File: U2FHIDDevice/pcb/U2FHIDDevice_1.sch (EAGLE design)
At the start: 32 parts, among them CN1 TE-1734028, CN2 IF_7PIN, SW1 SKRPACE010, U1 STM32F411RET6_, U2 LD39050PU33R_DEV, U3 USBLC6-2SC6, X1 NX3215SA_

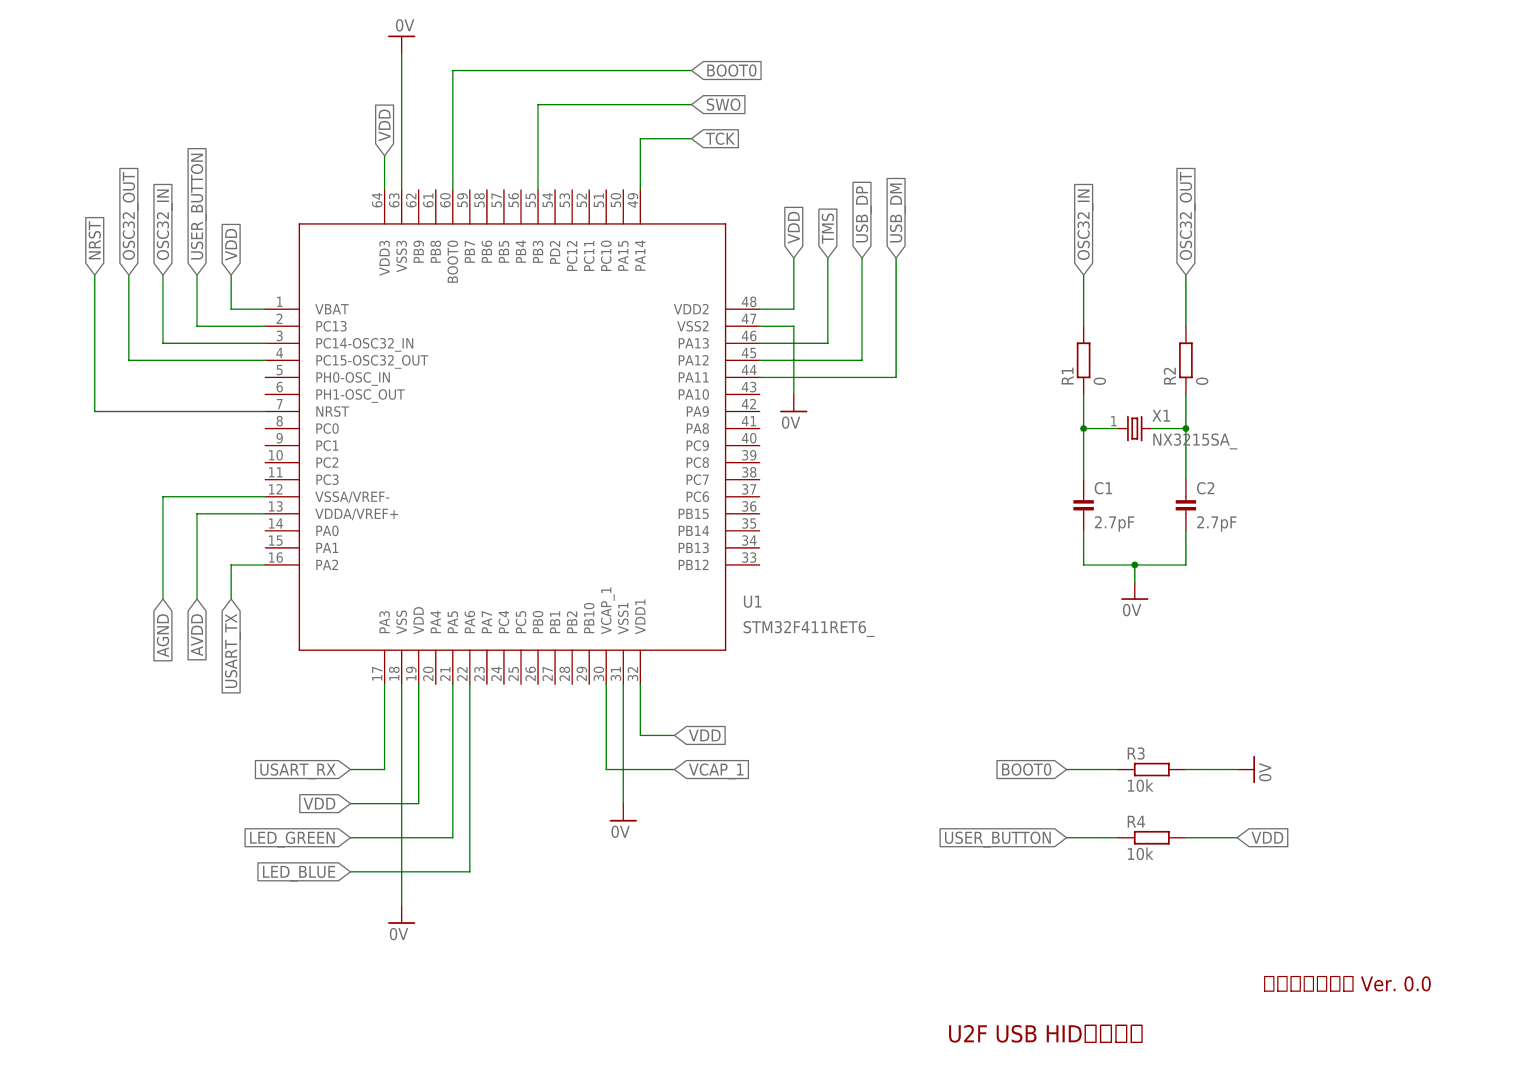
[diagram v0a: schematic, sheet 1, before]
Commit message: 回路修正
・8MHzクリスタルを追加
・それに伴い、基板レイアウトを大幅に修正
（部品が大きく、前回レイアウトがベースだと配置できないための措置）
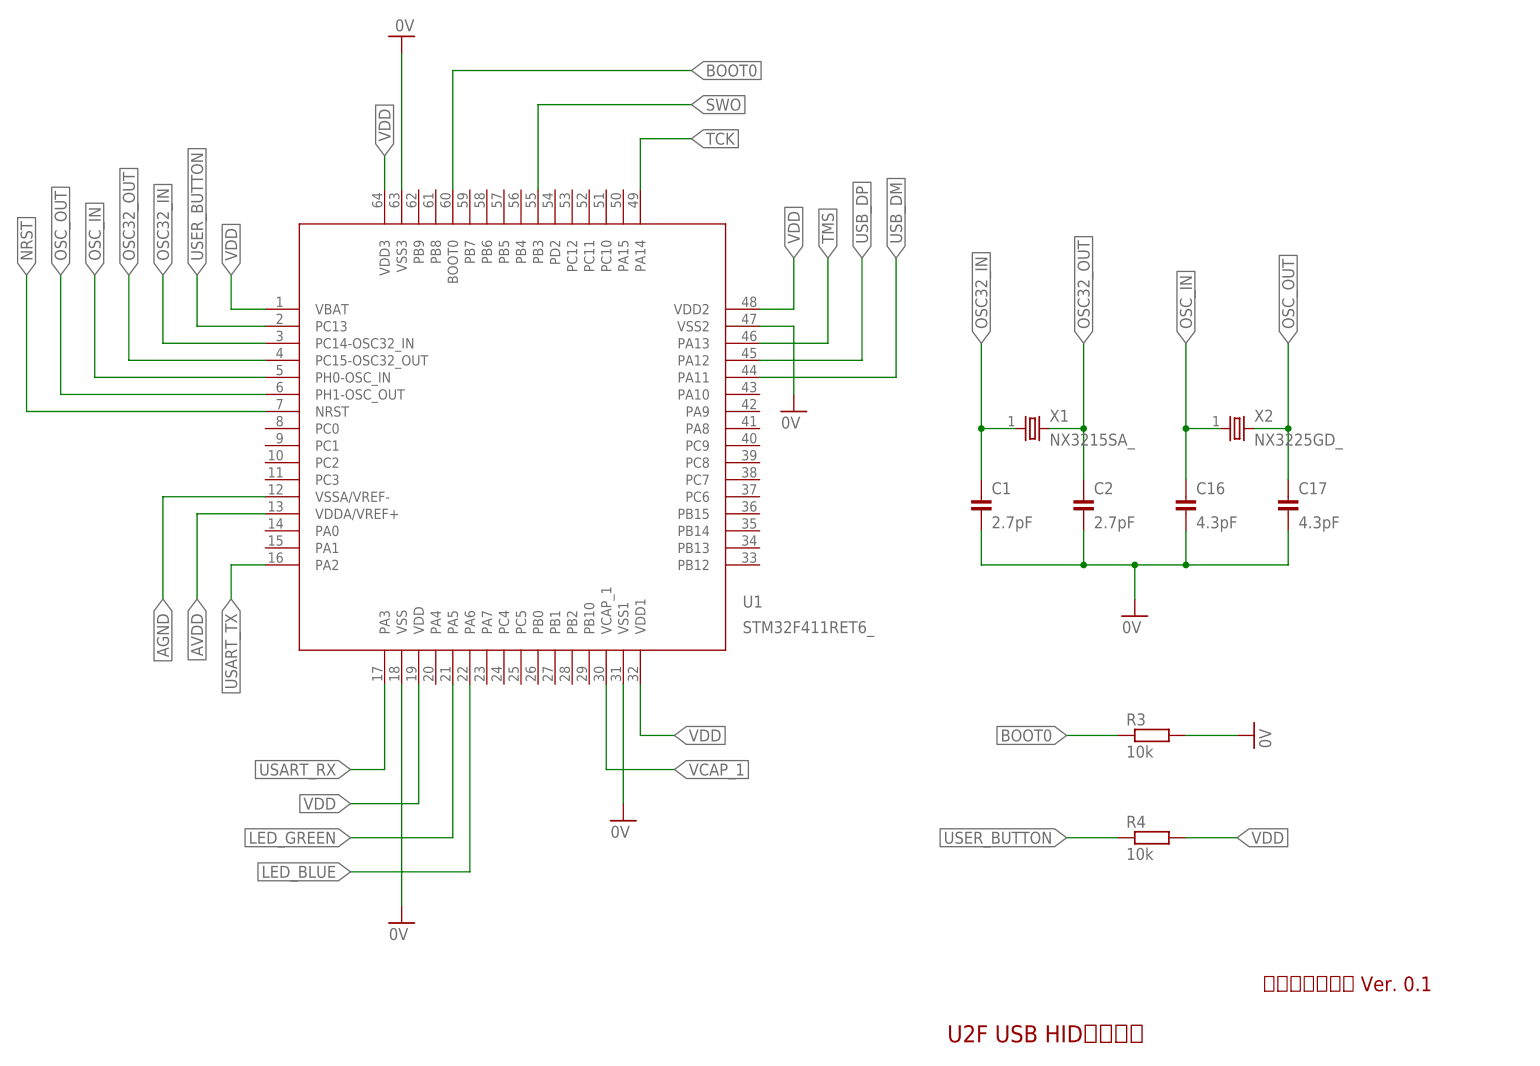
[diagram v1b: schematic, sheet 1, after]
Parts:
- removed R1, R2: 0, Parts:RESISTOR_0603
- added C16, C17: 4.3pF, Parts:CAP_0603
- added X2: NX3225GD_, Parts:NX3225GD_
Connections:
- removed net N$2: C1.1, R1.1, X1.1
- removed net N$3: C2.1, R2.1, X1.2
- new net OSC_IN: C16.1, U1.PH0-OSC_IN, X2.1
- new net OSC_OUT: C17.1, U1.PH1-OSC_OUT, X2.2
- net 0V: now also C16.2, C17.2
- net OSC32_IN: now also C1.1, X1.1; no longer R1.2
- net OSC32_OUT: now also C2.1, X1.2; no longer R2.2
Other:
- note added: "試作基板回路図 Ver. 0.1"
- note removed: "試作基板回路図 Ver. 0.0"
- moved on the sheet: C1, C2, R3, R5, X1

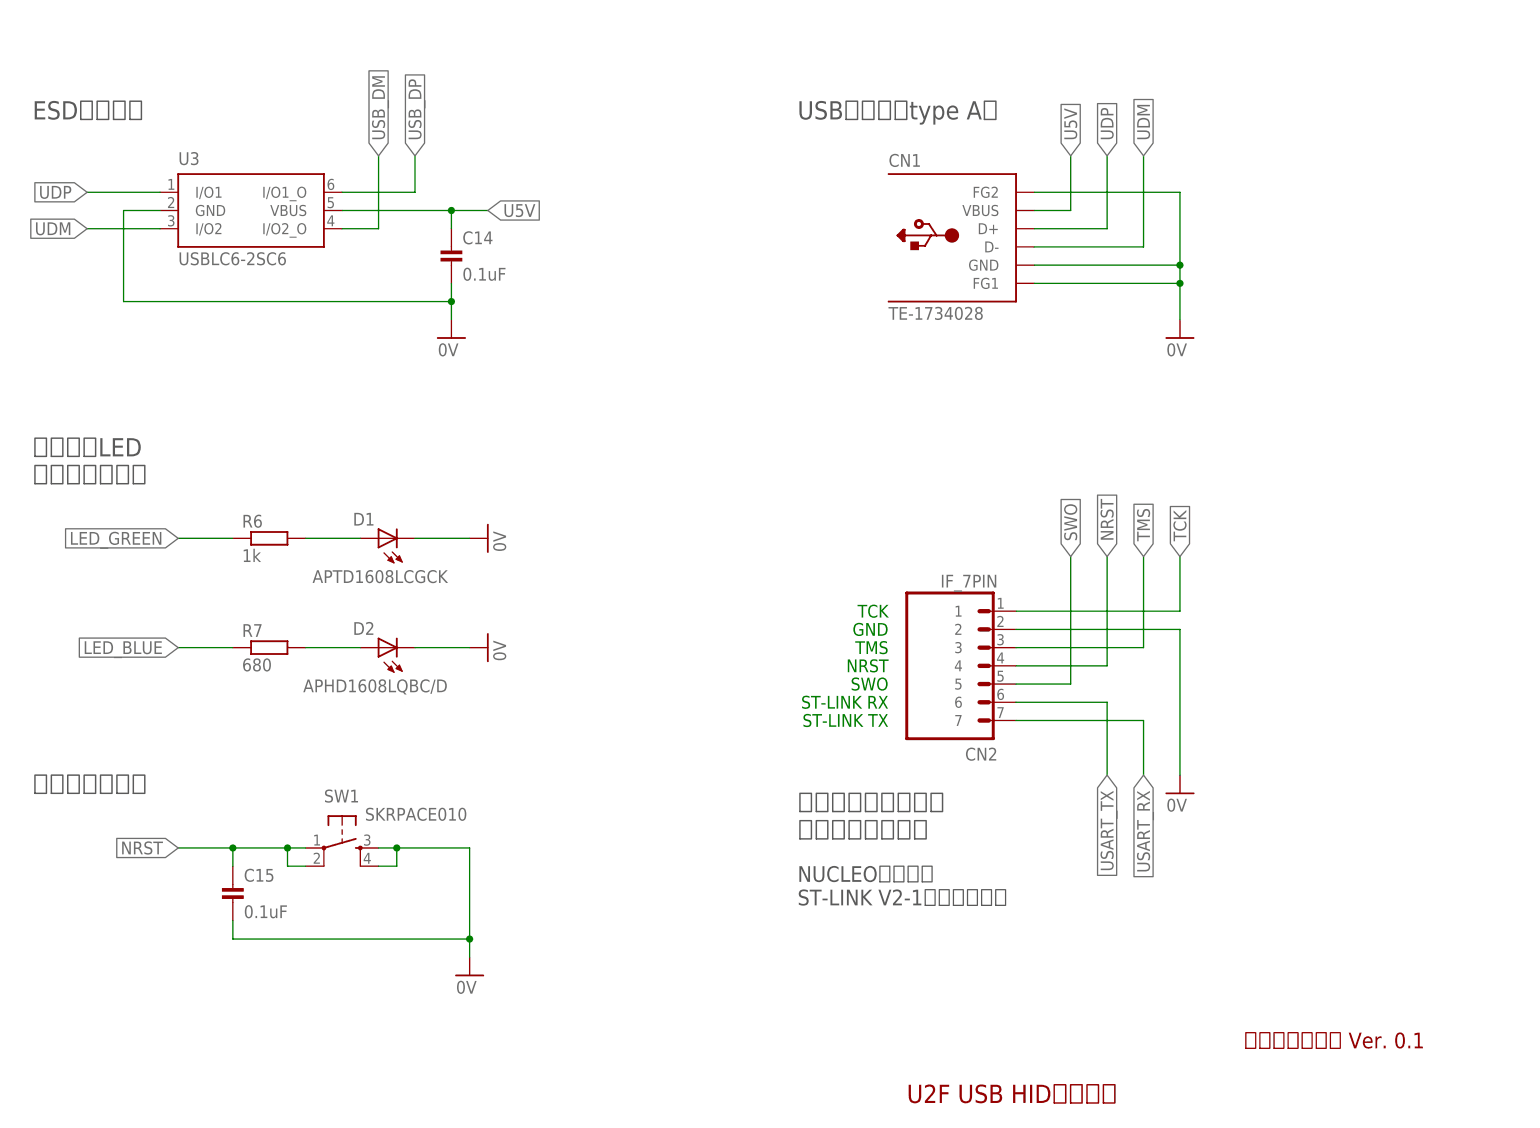
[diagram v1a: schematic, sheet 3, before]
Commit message: 基板レイアウト修正
・ユーザースイッチを追加（回路はNUCLEOが参考）
・ST-LINK V2-1インターフェースピンのレイアウトが逆だったので修正
・基板サイズは修正なし
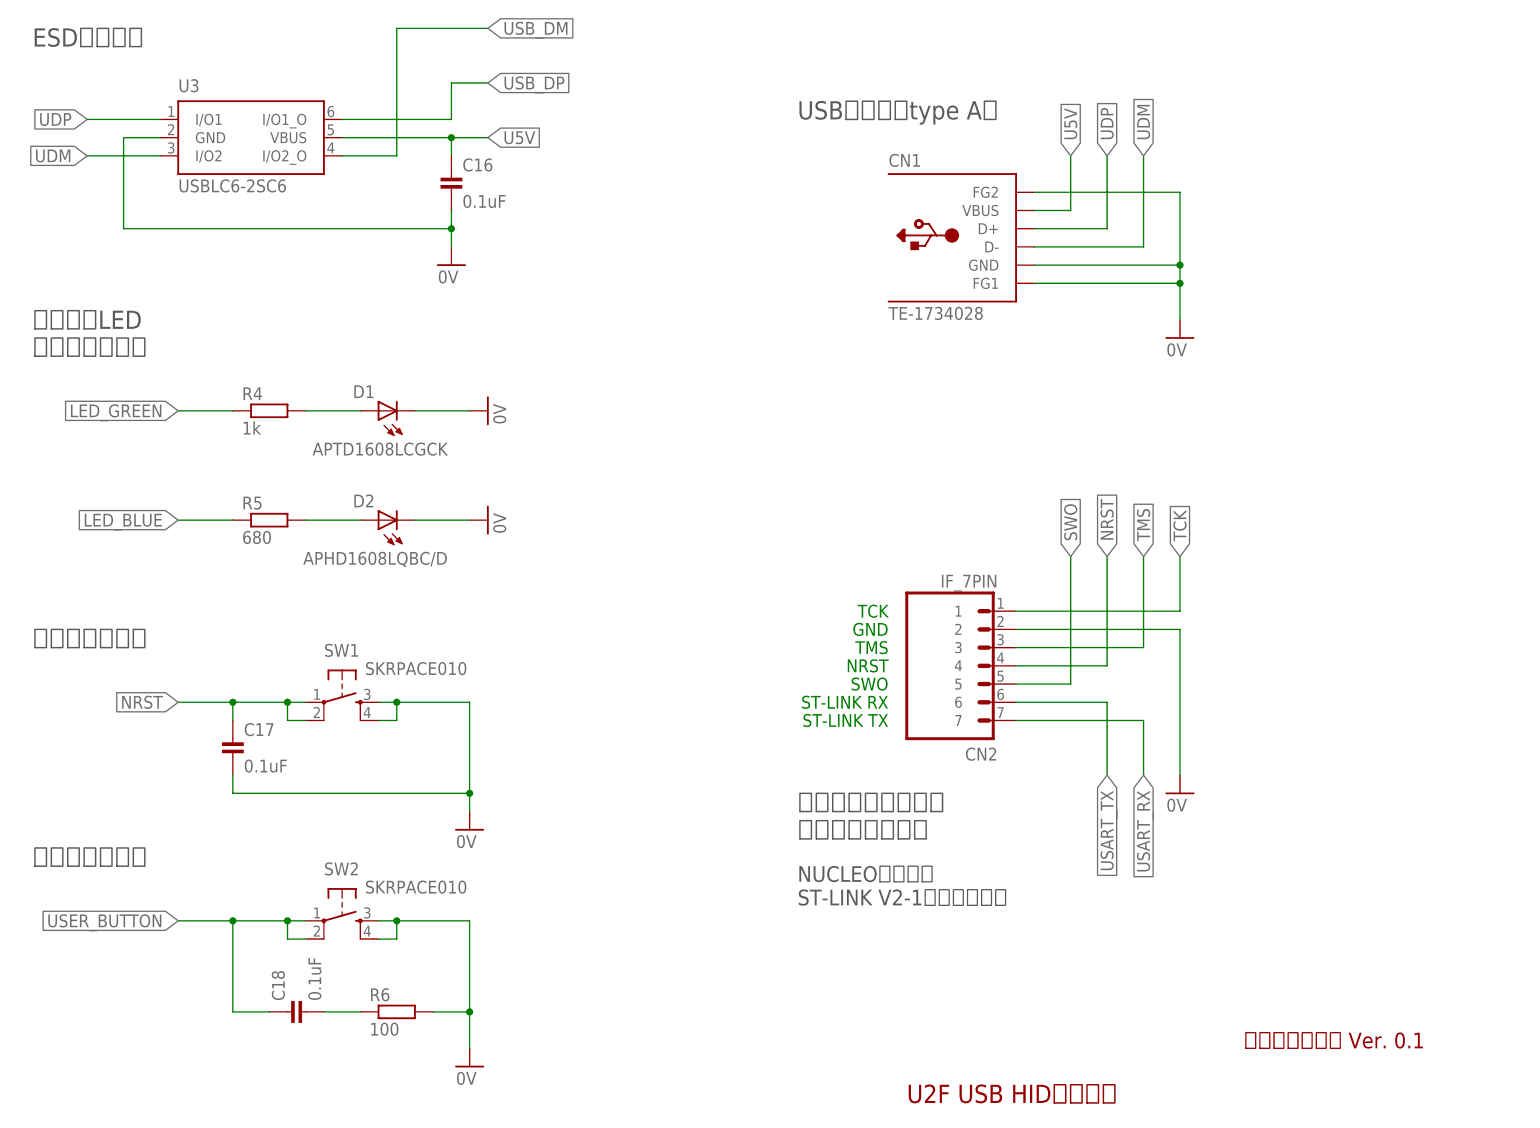
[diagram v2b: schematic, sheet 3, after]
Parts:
- removed R7: 680, Parts:RESISTOR_0603
- added C18: 0.1uF, Parts:CAP_0603
- added R1: 10k, Parts:RESISTOR_0603
- added R2: 4.7k, Parts:RESISTOR_0603
- added SW2: SKRPACE010, Parts:SKRPACE010
- C11: value 1uF -> 0.1uF
- C12: value 4.7uF -> 0.1uF; device Parts:CAP_1206 -> Parts:CAP_0603
- C13, C7: value 0.1uF -> 1uF
- C14: value 0.1uF -> 4.7uF; device Parts:CAP_0603 -> Parts:CAP_1206
- C16, C17: value 4.3pF -> 0.1uF
- C3: value 1uF -> 4.3pF
- C4: value 0.1uF -> 4.3pF
- R3: value 10k -> 0
- R4: value 10k -> 1k
- R5: value 0 -> 680
- R6: value 1k -> 100
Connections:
- new net N$2: C18.2, R6.1
- net 0V: now also C13.2, R1.2, R3.1, R6.2, SW2.S, SW2.S1; no longer C15.2, R3.2, R5.1
- net AGND: now also C15.2, R3.2; no longer C13.2, R5.2
- net AVDD: now also C15.1; no longer C13.1
- net BOOT0: now also R1.1; no longer R3.1
- net LED_BLUE: now also R5.1; no longer R7.1
- net LED_GREEN: now also R4.1; no longer R6.1
- net N$1: now also R4.2; no longer R6.2
- net N$4: now also R5.2; no longer R7.2
- net NRST: now also C17.1; no longer C15.1
- net OSC_IN: now also C3.1; no longer C16.1
- net OSC_OUT: now also C4.1; no longer C17.1
- net U5V: now also C16.1, C5.1, C6.1; no longer C14.1, C3.1, C4.1
- net USER_BUTTON: now also C18.1, R2.1, SW2.P, SW2.P1; no longer R4.1
- net VCAP_1: now also C14.1; no longer C12.1
- net VDD: now also C12.1, C13.1, R2.2; no longer C5.1, C6.1, R4.2
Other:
- note added: "ユーザーボタン"
- moved on the sheet: C10, C11, C12, C13, C5, C6, C7, C8, C9, D1, D2, R6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
